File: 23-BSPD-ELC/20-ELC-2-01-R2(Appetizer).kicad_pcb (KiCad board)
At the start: 2 copper layers, 58 x 73 mm, 82 parts, among them J1 Conn_01x05, J2 Conn_01x03, SW1 UK-B0288-SP25Y, U1 LM239, U10 CD4043BDR, U2 LM239, U5 LM239, U6 SN74HC32PWR, U7 74HC04, U8 74HC08D,653, U9 74LVC2G17

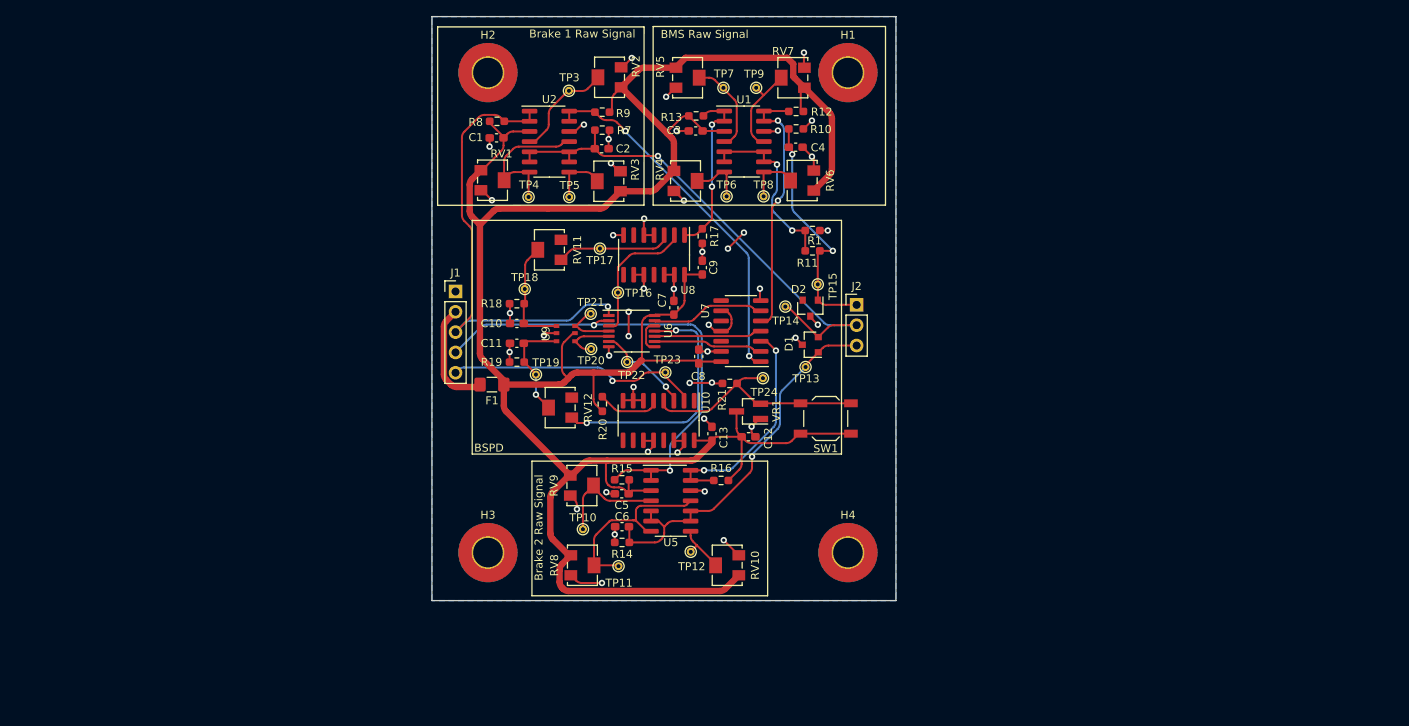
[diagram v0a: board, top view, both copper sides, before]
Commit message: Updated pcb layout; Watchdog on board still in progress
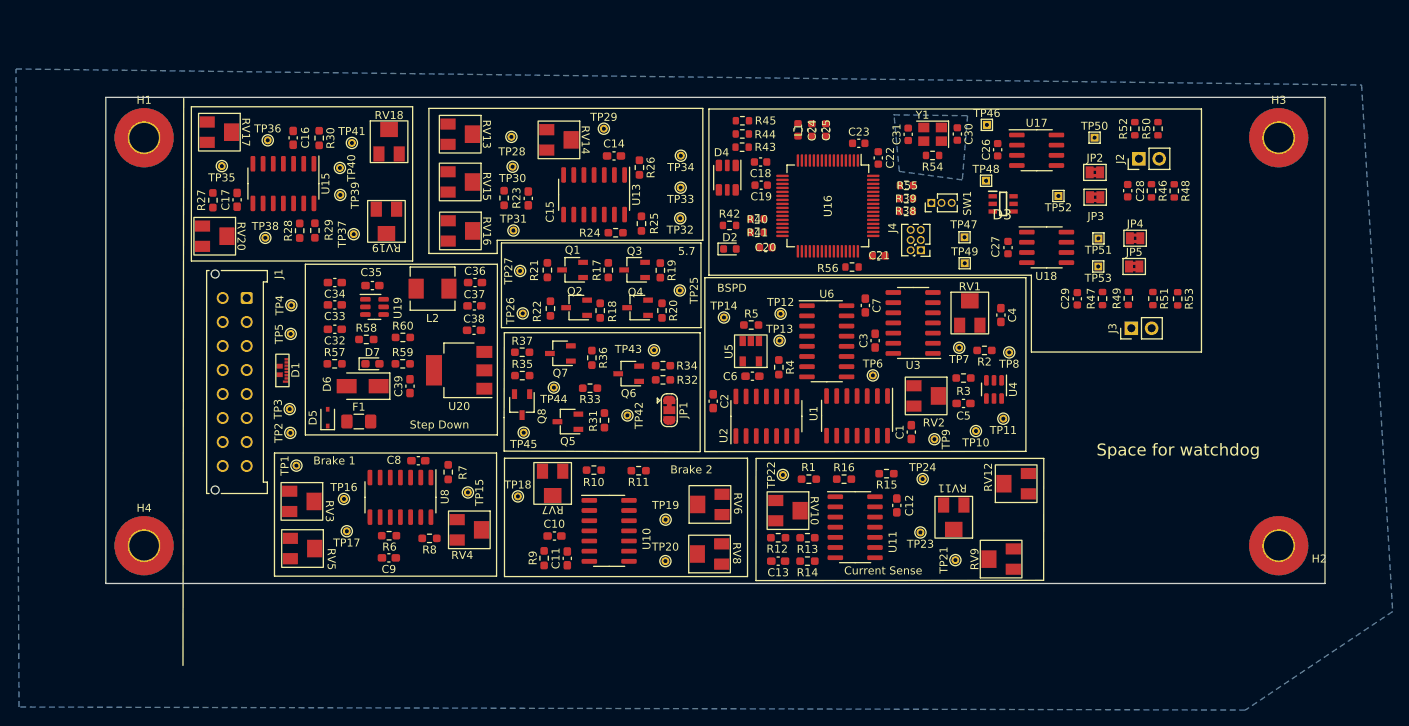
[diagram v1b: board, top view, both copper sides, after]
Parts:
- removed U7: 74HC04, Package_SO:SO-14_3.9x8.65mm_P1.27mm
- removed U9: 74LVC2G17, LHRE Footprint Library:74LVC2G17
- removed VR1: IMP810JEUR_T, Package_TO_SOT_SMD:SOT-23_Handsoldering
- added C14: 0.1uF, Capacitor_SMD:C_0603_1608Metric_Pad1.08x0.95mm_HandSolder, F.Cu at (130.8, 69.4)
- added C15: 0.1uF, Capacitor_SMD:C_0603_1608Metric_Pad1.08x0.95mm_HandSolder, F.Cu at (120.0, 74.7)
- added C16: 0.1uF, Capacitor_SMD:C_0603_1608Metric_Pad1.08x0.95mm_HandSolder, F.Cu at (90.7, 67.2)
- added C17: 0.1uF, Capacitor_SMD:C_0603_1608Metric_Pad1.08x0.95mm_HandSolder, F.Cu at (83.6, 74.9)
- added C18: 4u7, Capacitor_SMD:C_0603_1608Metric, F.Cu at (149.1, 70.2)
- added C19: 100n, Capacitor_SMD:C_0603_1608Metric, F.Cu at (149.2, 73.1)
- added C20: 100n, Capacitor_SMD:C_0603_1608Metric, F.Cu at (149.7, 80.9)
- added C21: 100n, Capacitor_SMD:C_0603_1608Metric, F.Cu at (163.8, 81.9)
- added C22: 100n, Capacitor_SMD:C_0603_1608Metric, F.Cu at (163.8, 69.7)
- added C23: 100n, Capacitor_SMD:C_0603_1608Metric, F.Cu at (161.4, 67.8)
- added C24: 1u, Capacitor_SMD:C_0603_1608Metric, F.Cu at (155.5, 66.2)
- added C25: 10n, Capacitor_SMD:C_0603_1608Metric, F.Cu at (157.2, 66.2)
- added C26: 0u1, Capacitor_SMD:C_0603_1608Metric, F.Cu at (178.7, 68.6)
- added C27: 0u1, Capacitor_SMD:C_0603_1608Metric, F.Cu at (180.0, 80.9)
- added C28: 4.7n, Capacitor_SMD:C_0603_1608Metric, F.Cu at (195.0, 73.8)
- added C29: 4.7n, Capacitor_SMD:C_0603_1608Metric, F.Cu at (188.7, 87.3)
- added C30: 10p, Capacitor_SMD:C_0603_1608Metric, F.Cu at (173.7, 66.7)
- added C31: 10p, Capacitor_SMD:C_0603_1608Metric, F.Cu at (167.5, 66.7)
- added C32: 10uF, Capacitor_SMD:C_0603_1608Metric_Pad1.08x0.95mm_HandSolder, F.Cu at (95.9, 91.1)
- added C33: 10uF, Capacitor_SMD:C_0603_1608Metric_Pad1.08x0.95mm_HandSolder, F.Cu at (95.9, 88.0)
- added C34: 100nF, Capacitor_SMD:C_0603_1608Metric_Pad1.08x0.95mm_HandSolder, F.Cu at (95.9, 85.2)
- added C35: 100nF, Capacitor_SMD:C_0603_1608Metric_Pad1.08x0.95mm_HandSolder, F.Cu at (100.6, 85.6)
- added C36: 22uF, Capacitor_SMD:C_0603_1608Metric_Pad1.08x0.95mm_HandSolder, F.Cu at (113.4, 85.2)
- added C37: 22uF, Capacitor_SMD:C_0603_1608Metric_Pad1.08x0.95mm_HandSolder, F.Cu at (113.3, 88.2)
- added C38: 1uF, Capacitor_SMD:C_0603_1608Metric_Pad1.08x0.95mm_HandSolder, F.Cu at (113.3, 91.2)
- added C39: 22uF, Capacitor_SMD:C_0603_1608Metric_Pad1.08x0.95mm_HandSolder, F.Cu at (105.3, 98.2)
- added D3: DT1446-04TS-7, Global Libraries:SOT95P280X100-6N, F.Cu at (179.4, 75.4)
- added D4: SMLVN6RGB, LED_SMD:LED_ROHM_SMLVN6, F.Cu at (144.9, 72.1)
- added D5: 32V, Diode_SMD:D_SOD-323, F.Cu at (95.0, 102.1)
- added D6: 0.7dV, Diode_SMD:D_SMA, F.Cu at (99.3, 98.2)
- added D7: LED, LED_SMD:LED_0603_1608Metric_Pad1.05x0.95mm_HandSolder, F.Cu at (100.6, 95.4)
- added J3: Conn_01x02, Connector_PinHeader_2.54mm:PinHeader_1x02_P2.54mm_Vertical, F.Cu at (195.4, 91.0)
- added J4: SWD, Connector_PinHeader_1.27mm:PinHeader_2x03_P1.27mm_Vertical, F.Cu at (169.1, 81.2)
- added JP1: Jumper_3_Bridged12, Jumper:SolderJumper-3_P1.3mm_Bridged12_RoundedPad1.0x1.5mm, F.Cu at (137.7, 101.2)
- added JP2: , Jumper:SolderJumper-2_P1.3mm_Bridged2Bar_Pad1.0x1.5mm, F.Cu at (190.9, 71.5)
- added JP3: , Jumper:SolderJumper-2_P1.3mm_Bridged2Bar_Pad1.0x1.5mm, F.Cu at (190.9, 74.6)
- added JP4: , Jumper:SolderJumper-2_P1.3mm_Bridged2Bar_Pad1.0x1.5mm, F.Cu at (195.9, 79.7)
- added JP5: , Jumper:SolderJumper-2_P1.3mm_Bridged2Bar_Pad1.0x1.5mm, F.Cu at (195.8, 83.2)
- added L1: 68n, Inductor_SMD:L_0603_1608Metric, F.Cu at (153.8, 66.2)
- added L2: 4u7, Inductor_SMD:L_Sunlord_MWSA0518_5.4x5.2mm, F.Cu at (108.1, 86.0)
- added Q1: Q_PMOS_GSD, Package_TO_SOT_SMD:TSOT-23, F.Cu at (125.6, 83.7)
- added Q2: Q_PMOS_GSD, Package_TO_SOT_SMD:TSOT-23, F.Cu at (126.1, 88.4)
- added Q3: Q_NMOS_GSD-Device, Package_TO_SOT_SMD:TSOT-23, F.Cu at (133.3, 83.7)
- added Q4: Q_NMOS_GSD-Device, Package_TO_SOT_SMD:TSOT-23, F.Cu at (133.7, 88.4)
- added Q5: Q_NMOS_GSD-Device, Package_TO_SOT_SMD:TSOT-23, F.Cu at (125.0, 102.6)
- added Q6: Q_NMOS_GSD-Device, Package_TO_SOT_SMD:TSOT-23, F.Cu at (132.6, 96.6)
- added Q7: Q_PMOS_DSG, Package_TO_SOT_SMD:TSOT-23, F.Cu at (124.1, 94.1)
- added Q8: Q_PMOS_DSG, Package_TO_SOT_SMD:TSOT-23, F.Cu at (119.3, 100.5)
- added R2: 10k, Resistor_SMD:R_0603_1608Metric_Pad0.98x0.95mm_HandSolder, F.Cu at (177.1, 93.7)
- added R22: 10k, Resistor_SMD:R_0603_1608Metric_Pad0.98x0.95mm_HandSolder, F.Cu at (122.8, 88.5)
- added R23: 510, Resistor_SMD:R_0603_1608Metric_Pad0.98x0.95mm_HandSolder, F.Cu at (117.0, 74.7)
- added R24: 10k, Resistor_SMD:R_0603_1608Metric_Pad0.98x0.95mm_HandSolder, F.Cu at (131.0, 79.0)
- added R25: 10k, Resistor_SMD:R_0603_1608Metric_Pad0.98x0.95mm_HandSolder, F.Cu at (134.2, 77.9)
- added R26: 10k, Resistor_SMD:R_0603_1608Metric_Pad0.98x0.95mm_HandSolder, F.Cu at (133.9, 70.9)
- added R27: 510, Resistor_SMD:R_0603_1608Metric_Pad0.98x0.95mm_HandSolder, F.Cu at (80.6, 75.0)
- added R28: 10k, Resistor_SMD:R_0603_1608Metric_Pad0.98x0.95mm_HandSolder, F.Cu at (91.5, 78.8)
- added R29: 10k, Resistor_SMD:R_0603_1608Metric_Pad0.98x0.95mm_HandSolder, F.Cu at (93.4, 78.7)
- added R3: 10k, Resistor_SMD:R_0603_1608Metric_Pad0.98x0.95mm_HandSolder, F.Cu at (174.4, 97.2)
- added R30: 10k, Resistor_SMD:R_0603_1608Metric_Pad0.98x0.95mm_HandSolder, F.Cu at (93.9, 67.2)
- added R31: 25, Resistor_SMD:R_0603_1608Metric_Pad0.98x0.95mm_HandSolder, F.Cu at (129.6, 102.5)
- added R32: 25, Resistor_SMD:R_0603_1608Metric_Pad0.98x0.95mm_HandSolder, F.Cu at (136.9, 97.4)
- added R33: 10k, Resistor_SMD:R_0603_1608Metric_Pad0.98x0.95mm_HandSolder, F.Cu at (127.8, 98.5)
- added R34: 10k, Resistor_SMD:R_0603_1608Metric_Pad0.98x0.95mm_HandSolder, F.Cu at (136.9, 95.6)
- added R35: 10k, Resistor_SMD:R_0603_1608Metric_Pad0.98x0.95mm_HandSolder, F.Cu at (119.3, 96.9)
- added R36: 10k, Resistor_SMD:R_0603_1608Metric_Pad0.98x0.95mm_HandSolder, F.Cu at (128.0, 94.7)
- added R37: 25, Resistor_SMD:R_0603_1608Metric_Pad0.98x0.95mm_HandSolder, F.Cu at (119.3, 94.0)
- added R38: 2k2, Resistor_SMD:R_0603_1608Metric, F.Cu at (167.3, 76.3)
- added R39: 2k2, Resistor_SMD:R_0603_1608Metric, F.Cu at (167.3, 74.7)
- added R4: 10k, Resistor_SMD:R_0603_1608Metric_Pad0.98x0.95mm_HandSolder, F.Cu at (151.4, 95.8)
- added R40: 2k2, Resistor_SMD:R_0603_1608Metric, F.Cu at (148.7, 77.3)
- added R41: 2k2, Resistor_SMD:R_0603_1608Metric, F.Cu at (148.7, 79.0)
- added R42: 100, Resistor_SMD:R_0603_1608Metric, F.Cu at (145.2, 78.1)
- added R43: 220, Resistor_SMD:R_0603_1608Metric, F.Cu at (146.8, 68.3)
- added R44: 220, Resistor_SMD:R_0603_1608Metric, F.Cu at (146.8, 66.7)
- added R45: 220, Resistor_SMD:R_0603_1608Metric, F.Cu at (146.8, 65.0)
- added R46: 120, Resistor_SMD:R_0603_1608Metric, F.Cu at (197.9, 73.8)
- added R47: 120, Resistor_SMD:R_0603_1608Metric, F.Cu at (191.8, 87.2)
- added R48: 120, Resistor_SMD:R_0603_1608Metric, F.Cu at (200.8, 73.8)
- added R49: 120, Resistor_SMD:R_0603_1608Metric, F.Cu at (195.0, 87.2)
- added R5: 100k, Resistor_SMD:R_0603_1608Metric_Pad0.98x0.95mm_HandSolder, F.Cu at (147.9, 90.6)
- added R50: 120, Resistor_SMD:R_0603_1608Metric, F.Cu at (198.8, 66.0)
- added R51: 120, Resistor_SMD:R_0603_1608Metric, F.Cu at (198.1, 87.2)
- added R52: 120, Resistor_SMD:R_0603_1608Metric, F.Cu at (195.9, 66.0)
- added R53: 120, Resistor_SMD:R_0603_1608Metric, F.Cu at (201.2, 87.3)
- added R54: 47, Resistor_SMD:R_0603_1608Metric, F.Cu at (170.6, 69.4)
- added R55: 10K, Resistor_SMD:R_0603_1608Metric, F.Cu at (167.3, 73.1)
- added R56: 22, Resistor_SMD:R_0603_1608Metric, F.Cu at (160.5, 83.3)
- added R57: 470R, Resistor_SMD:R_0603_1608Metric_Pad0.98x0.95mm_HandSolder, F.Cu at (95.8, 95.4)
- added R58: 10K, Resistor_SMD:R_0603_1608Metric_Pad0.98x0.95mm_HandSolder, F.Cu at (99.8, 92.4)
- added R59: 10K, Resistor_SMD:R_0603_1608Metric_Pad0.98x0.95mm_HandSolder, F.Cu at (104.3, 95.4)
- added R6: 510k, Resistor_SMD:R_0603_1608Metric_Pad0.98x0.95mm_HandSolder, F.Cu at (102.6, 116.9)
- added R60: 54.9K, Resistor_SMD:R_0603_1608Metric_Pad0.98x0.95mm_HandSolder, F.Cu at (104.4, 92.1)
- added RV13: 10k, Global Libraries:PVG5A, F.Cu at (111.5, 66.7)
- added RV14: 10k, Global Libraries:PVG5A, F.Cu at (123.9, 67.4)
- added RV15: R_POT_TRIM-Device, Global Libraries:PVG5A, F.Cu at (111.5, 72.7)
- added RV16: R_POT_TRIM-Device, Global Libraries:PVG5A, F.Cu at (111.6, 78.8)
- added RV17: 10k, Global Libraries:PVG5A, F.Cu at (81.4, 66.4)
- added RV18: 10k, Global Libraries:PVG5A, F.Cu at (102.6, 67.6)
- added RV19: R_POT_TRIM-Device, Global Libraries:PVG5A, F.Cu at (102.3, 77.6)
- added RV20: R_POT_TRIM-Device, Global Libraries:PVG5A, F.Cu at (80.8, 79.5)
- added TP1: TestPoint-Connector, TestPoint:TestPoint_THTPad_D1.0mm_Drill0.5mm, F.Cu at (91.1, 108.1)
- added TP2: TestPoint-Connector, TestPoint:TestPoint_THTPad_D1.0mm_Drill0.5mm, F.Cu at (90.3, 104.0)
- added TP25: TestPoint, TestPoint:TestPoint_THTPad_D1.0mm_Drill0.5mm, F.Cu at (139.0, 86.2)
- added TP26: TestPoint-Connector, TestPoint:TestPoint_THTPad_D1.0mm_Drill0.5mm, F.Cu at (119.4, 89.1)
- added TP27: TestPoint-Connector, TestPoint:TestPoint_THTPad_D1.0mm_Drill0.5mm, F.Cu at (119.0, 83.8)
- added TP28: TestPoint, TestPoint:TestPoint_THTPad_D1.0mm_Drill0.5mm, F.Cu at (117.9, 67.0)
- added TP29: TestPoint, TestPoint:TestPoint_THTPad_D1.0mm_Drill0.5mm, F.Cu at (129.5, 66.0)
- added TP30: TestPoint, TestPoint:TestPoint_THTPad_D1.0mm_Drill0.5mm, F.Cu at (118.1, 70.8)
- added TP31: TestPoint, TestPoint:TestPoint_THTPad_D1.0mm_Drill0.5mm, F.Cu at (118.2, 78.7)
- added TP32: TestPoint, TestPoint:TestPoint_THTPad_D1.0mm_Drill0.5mm, F.Cu at (139.0, 77.2)
- added TP33: TestPoint, TestPoint:TestPoint_THTPad_D1.0mm_Drill0.5mm, F.Cu at (139.1, 73.4)
- added TP34: TestPoint, TestPoint:TestPoint_THTPad_D1.0mm_Drill0.5mm, F.Cu at (139.1, 69.4)
- added TP35: TestPoint, TestPoint:TestPoint_THTPad_D1.0mm_Drill0.5mm, F.Cu at (81.7, 70.7)
- added TP36: TestPoint, TestPoint:TestPoint_THTPad_D1.0mm_Drill0.5mm, F.Cu at (87.5, 67.5)
- added TP37: TestPoint, TestPoint:TestPoint_THTPad_D1.0mm_Drill0.5mm, F.Cu at (98.2, 79.2)
- added TP38: TestPoint, TestPoint:TestPoint_THTPad_D1.0mm_Drill0.5mm, F.Cu at (87.2, 79.7)
- added TP39: TestPoint, TestPoint:TestPoint_THTPad_D1.0mm_Drill0.5mm, F.Cu at (96.5, 74.3)
- added TP40: TestPoint, TestPoint:TestPoint_THTPad_D1.0mm_Drill0.5mm, F.Cu at (96.5, 70.9)
- added TP41: TestPoint, TestPoint:TestPoint_THTPad_D1.0mm_Drill0.5mm, F.Cu at (98.0, 67.8)
- added TP42: TestPoint-Connector, TestPoint:TestPoint_THTPad_D1.0mm_Drill0.5mm, F.Cu at (132.4, 101.9)
- added TP43: TestPoint-Connector, TestPoint:TestPoint_THTPad_D1.0mm_Drill0.5mm, F.Cu at (135.8, 93.7)
- added TP44: TestPoint-Connector, TestPoint:TestPoint_THTPad_D1.0mm_Drill0.5mm, F.Cu at (123.2, 98.4)
- added TP45: TestPoint-Connector, TestPoint:TestPoint_THTPad_D1.0mm_Drill0.5mm, F.Cu at (119.5, 104.0)
- added TP46: , TestPoint:TestPoint_THTPad_1.0x1.0mm_Drill0.5mm, F.Cu at (177.4, 65.5)
- added TP47: , TestPoint:TestPoint_THTPad_1.0x1.0mm_Drill0.5mm, F.Cu at (174.6, 79.6)
- added TP48: , TestPoint:TestPoint_THTPad_1.0x1.0mm_Drill0.5mm, F.Cu at (177.3, 72.5)
- added TP49: , TestPoint:TestPoint_THTPad_1.0x1.0mm_Drill0.5mm, F.Cu at (174.6, 82.8)
- added TP50: , TestPoint:TestPoint_THTPad_1.0x1.0mm_Drill0.5mm, F.Cu at (190.8, 67.1)
- added TP51: , TestPoint:TestPoint_THTPad_1.0x1.0mm_Drill0.5mm, F.Cu at (191.3, 79.7)
- added TP52: , TestPoint:TestPoint_THTPad_1.0x1.0mm_Drill0.5mm, F.Cu at (186.3, 74.4)
- added TP53: , TestPoint:TestPoint_THTPad_1.0x1.0mm_Drill0.5mm, F.Cu at (191.3, 83.2)
- added U11: LM239, Package_SO:SO-14_3.9x8.65mm_P1.27mm, F.Cu at (160.9, 115.8)
- added U13: LM239, Package_SO:SO-14_3.9x8.65mm_P1.27mm, F.Cu at (128.3, 74.3)
- added U15: LM239, Package_SO:SO-14_3.9x8.65mm_P1.27mm, F.Cu at (89.4, 72.9)
- added U16: STM32F105RCTx, Package_QFP:LQFP-64_10x10mm_P0.5mm, F.Cu at (157.5, 75.7)
- added U17: SN65HVD230, Package_SO:SOIC-8_3.9x4.9mm_P1.27mm, F.Cu at (183.6, 68.7)
- added U18: SN65HVD230, Package_SO:SOIC-8_3.9x4.9mm_P1.27mm, F.Cu at (184.8, 80.8)
- added U19: LMR51420, Package_TO_SOT_SMD:SOT-23-6, F.Cu at (100.8, 88.3)
- added U20: AMS1117-3.3, Package_TO_SOT_SMD:SOT-223-3_TabPin2, F.Cu at (111.4, 96.2)
- added U3: 74HC08D,653, Package_SO:SOIC-14_3.9x8.7mm_P1.27mm, F.Cu at (168.1, 90.3)
- added U4: 74LVC2G17DBVE4, Package_TO_SOT_SMD:SOT-23-6, F.Cu at (178.3, 98.6)
- added Y1: 16MHz, Crystal:Crystal_SMD_3225-4Pin_3.2x2.5mm, F.Cu at (170.6, 66.7)
- C10, C11: value 1uF -> 0.1uF
- C4, C5: value 0.1uF -> 22uF
- D1: value PSM712-LF-T7 -> ESD7016MUTAG; footprint Package_TO_SOT_SMD:SOT-23 -> Global Libraries:ESD7016MUTAG
- D2: value PSM712-LF-T7 -> RED; footprint Package_TO_SOT_SMD:SOT-23 -> LED_SMD:LED_0603_1608Metric
- F1: value 1A -> 2A
- J1: value Conn_01x05 -> Conn_02x08_Counter_Clockwise; footprint Connector_PinHeader_2.54mm:PinHeader_1x05_P2.54mm_Vertical -> Connector_Molex:Molex_Micro-Fit_3.0_43045-1612_2x08_P3.00mm_Vertical
- J2: value Conn_01x03 -> Conn_01x02; footprint Connector_PinHeader_2.54mm:PinHeader_1x03_P2.54mm_Vertical -> Connector_PinHeader_2.54mm:PinHeader_1x02_P2.54mm_Vertical
- R1, R11: value 150 -> 10k
- R10, R7: value 510k -> 10k
- R12, R9: value 10k -> 510k
- R13: value 10k -> 150
- R14: value 510k -> 150
- R18, R19: value 10k -> 250
- RV1, RV10, RV11, RV12, RV2, RV3, RV4, RV5, RV6, RV7, RV8, RV9: footprint Potentiometer_SMD:Potentiometer_Bourns_3214W_Vertical -> Global Libraries:PVG5A
- SW1: value UK-B0288-SP25Y -> SW_SPDT; footprint Button_Switch_SMD:SW_SPST_TL3342 -> Connector_PinHeader_1.27mm:PinHeader_1x03_P1.27mm_Vertical
- TP3, TP4, TP5: value TestPoint -> TestPoint-Connector
- U1: value LM239 -> SN74ALS32DR; footprint Package_SO:SO-14_3.9x8.65mm_P1.27mm -> Package_SO:SOIC-14_3.9x8.7mm_P1.27mm
- U10: value CD4043BDR -> LM239; footprint Package_SO:SOIC-16_3.9x9.9mm_P1.27mm -> Package_SO:SO-14_3.9x8.65mm_P1.27mm
- U2: value LM239 -> 74HC04D,653
- U5: value LM239 -> APX823-44W5G-7; footprint Package_SO:SO-14_3.9x8.65mm_P1.27mm -> Global Libraries:AXP823-44W5G-7
- U6: value SN74HC32PWR -> CD4043BDR; footprint Package_SO:TSSOP-14_4.4x5mm_P0.65mm -> Package_SO:SOIC-16_3.9x9.9mm_P1.27mm
- U8: value 74HC08D,653 -> LM239; footprint Package_SO:SOIC-14_3.9x8.7mm_P1.27mm -> Package_SO:SO-14_3.9x8.65mm_P1.27mm
- moved H2 115.2 mm to (213.8, 118.1)
- moved H3 111.6 mm to (213.8, 67.1)
- moved H1 88.4 mm to (72.0, 67.1)
- moved H4 88.0 mm to (72.0, 118.1)
- moved RV5 76.0 mm to (91.8, 118.5), turned to -90 degrees
- moved D1 66.1 mm to (89.3, 96.2), turned to 90 degrees
- moved C1 63.6 mm to (167.9, 103.9), turned to 90 degrees
- moved RV1 61.9 mm to (175.2, 89.1), turned to 0 degrees
- moved RV11 60.6 mm to (173.2, 114.6), turned to 180 degrees
- moved RV7 58.9 mm to (123.1, 110.4), turned to 180 degrees
- moved RV12 57.8 mm to (181.0, 110.4), turned to 90 degrees
- moved R9 56.2 mm to (122.0, 119.7), turned to -90 degrees
- moved RV2 56.1 mm to (169.8, 99.4)
- moved RV3 55.4 mm to (91.7, 112.6)
- moved TP21 55.0 mm to (173.4, 119.9), turned to 90 degrees
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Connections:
- C10 pad 1: Net-(C10-Pad1) -> +5V
- C11 pad 1: Net-(C11-Pad1) -> /Brake2_Signal_Raw
- C13 pad 1: +5V -> /Current_Sense_Signal_Raw
- C2 pad 1: /Brake1_Signal_Raw -> +5V
- C4 pad 1: /BMS_Signal_Raw -> Net-(C4-Pad1)
- C5 pad 1: +5V -> Net-(C5-Pad1)
- C6 pad 1: /Brake2_Signal_Raw -> +5V
- C9 pad 1: +5V -> /Brake1_Signal_Raw
- D1 pad 1: /Brake2_Signal_Raw -> /Current_Sense_Signal_Raw
- D1 pad 2: /Brake1_Signal_Raw -> /Brake2_Signal_Raw
- D2 pad 1: /BMS_Signal_Raw -> Net-(D2-Pad1)
- D2 pad 2: unconnected-(D2-Pad2) -> +3V3
- F1 pad 1: +5V -> /24 to 5V Step Down/DIODE
- F1 pad 2: Net-(F1-Pad2) -> +24V
- J1 pad 1: GND -> +24V
- J1 pad 2: Net-(F1-Pad2) -> /APPs1_Signal_Raw
- J1 pad 3: /Brake1_Signal -> /APPs2_Signal_Raw
- J1 pad 4: /Brake2_Signal -> /Brake1_Signal_Raw
- J1 pad 5: /~{BSPD_TRIPPED} -> /Brake2_Signal_Raw
- J2 pad 1: /BMS_Signal_Raw -> Net-(C28-Pad2)
- J2 pad 2: /Brake1_Signal_Raw -> Net-(J2-Pad2)
- R1 pad 1: /BMS Signal/DataRaw_Half -> /CurrentSense_Signal
- R10 pad 1: GND -> /Brake2_Signal
- R10 pad 2: /BMS_Signal_Raw -> +5V
- R11 pad 1: /BMS Signal/DataRaw_Half -> +5V
- R11 pad 2: /BMS_Signal_Raw -> /Brake2_Connected
- R12 pad 1: /BMS_Connected -> GND
- R12 pad 2: +5V -> /Current_Sense_Signal_Raw
- R13 pad 1: +5V -> /BMS Signal/DataRaw_Half
- R13 pad 2: /BMS_Signal -> /Current_Sense_Signal_Raw
- R14 pad 1: GND -> /BMS Signal/DataRaw_Half
- R14 pad 2: /Brake2_Signal_Raw -> GND
- R15 pad 1: /Brake2_Signal -> /CurrentSense_Connected
- R16 pad 2: /Brake2_Connected -> /CurrentSense_Signal
- R17 pad 1: /BMS_Signal -> Net-(Q1-Pad1)
- R17 pad 2: GND -> /APPs1_Signal_Raw
- R18 pad 1: Net-(C10-Pad1) -> Net-(Q2-Pad1)
- R18 pad 2: GND -> /APPs2_Signal_Raw
- R19 pad 1: Net-(C11-Pad1) -> GND
- R19 pad 2: GND -> /5.7/APPS_Trip
- R20 pad 1: Net-(R20-Pad1) -> GND
- R20 pad 2: +5V -> /5.7/APPS_Trip
- R21 pad 1: /BrakeSystemPlausibilityDevice/SET -> GND
- R21 pad 2: GND -> /APPs1_Out
- R7 pad 1: GND -> /Brake1_Signal
- R7 pad 2: /Brake1_Signal_Raw -> +5V
- R8 pad 1: /Brake1_Signal -> +5V
- R8 pad 2: +5V -> /Brake1_Connected
- R9 pad 1: +5V -> GND
- R9 pad 2: /Brake1_Connected -> /Brake2_Signal_Raw
- RV1 pad 1: +5V -> /BrakeSystemPlausibilityDevice/Power_and_Brakes
- RV1 pad 2: /Brake1 Signal/Vref_4V -> Net-(C4-Pad1)
- RV1 pad 3: GND -> unconnected-(RV1-Pad3)
- RV11 pad 1: /BrakeSystemPlausibilityDevice/Power_and_Brakes -> +5V
- RV11 pad 2: Net-(C10-Pad1) -> Net-(RV11-Pad2)
- RV11 pad 3: unconnected-(RV11-Pad3) -> GND
- RV12 pad 1: /BrakeSystemPlausibilityDevice/Signal_Lost -> +5V
- RV12 pad 2: Net-(C11-Pad1) -> Net-(RV12-Pad2)
- RV12 pad 3: unconnected-(RV12-Pad3) -> GND
- RV2 pad 1: +5V -> /BrakeSystemPlausibilityDevice/Signal_Lost
- RV2 pad 2: Net-(RV2-Pad2) -> Net-(C5-Pad1)
- RV2 pad 3: GND -> unconnected-(RV2-Pad3)
- RV3 pad 2: Net-(RV3-Pad2) -> /Brake1 Signal/Vref_4V
- RV6 pad 2: Net-(RV6-Pad2) -> /Brake2 Signal/Vref_4V
- RV8 pad 2: /Brake2 Signal/Vref_4V -> Net-(RV8-Pad2)
- SW1 pad 1: +5V -> +3V3
- SW1 pad 2: /BrakeSystemPlausibilityDevice/SET -> Net-(R55-Pad1)
- TP10 pad 1: Net-(RV9-Pad2) -> /BrakeSystemPlausibilityDevice/Signal_Lost_TRIP
- TP11 pad 1: /Brake2 Signal/Vref_4V -> /BrakeSystemPlausibilityDevice/Power_and_Brakes_TRIP
- TP12 pad 1: Net-(RV10-Pad2) -> /BrakeSystemPlausibilityDevice/TRIP
- TP13 pad 1: /Brake2_Signal_Raw -> /BrakeSystemPlausibilityDevice/SET
- TP14 pad 1: /Brake1_Signal_Raw -> /~{BSPD_TRIPPED}
- TP15 pad 1: /BMS_Signal_Raw -> Net-(RV4-Pad2)
- TP16 pad 1: Net-(TP16-Pad1) -> /Brake1 Signal/Vref_4V
- TP17 pad 1: /BrakeSystemPlausibilityDevice/Power_and_Brakes -> Net-(RV5-Pad2)
- TP18 pad 1: Net-(C10-Pad1) -> Net-(RV7-Pad2)
- TP19 pad 1: Net-(C11-Pad1) -> /Brake2 Signal/Vref_4V
- TP20 pad 1: /BrakeSystemPlausibilityDevice/Signal_Lost_TRIP -> Net-(RV8-Pad2)
- TP21 pad 1: /BrakeSystemPlausibilityDevice/Power_and_Brakes_TRIP -> Net-(RV9-Pad2)
- TP22 pad 1: /BrakeSystemPlausibilityDevice/TRIP -> Net-(RV10-Pad2)
- TP23 pad 1: /~{BSPD_TRIPPED} -> Net-(RV11-Pad2)
- TP24 pad 1: /BrakeSystemPlausibilityDevice/SET -> Net-(RV12-Pad2)
- TP3 pad 1: Net-(RV2-Pad2) -> /Brake2_Signal_Raw
- TP4 pad 1: /Brake1 Signal/Vref_4V -> /APPs1_Signal_Raw
- TP5 pad 1: Net-(RV3-Pad2) -> /APPs2_Signal_Raw
- TP6 pad 1: Net-(RV4-Pad2) -> Net-(TP6-Pad1)
- TP7 pad 1: Net-(RV5-Pad2) -> /BrakeSystemPlausibilityDevice/Power_and_Brakes
- TP8 pad 1: Net-(RV6-Pad2) -> Net-(C4-Pad1)
- TP9 pad 1: Net-(RV7-Pad2) -> Net-(C5-Pad1)
- U1 pad 1: /BMS_Signal -> /Brake1_Signal
- U1 pad 10: /BMS Signal/DataRaw_Half -> /BrakeSystemPlausibilityDevice/~{Brake2_Connected}
- U1 pad 11: Net-(RV7-Pad2) -> /BrakeSystemPlausibilityDevice/Signal_Lost
- U1 pad 12: GND -> /BrakeSystemPlausibilityDevice/~{Brake_Connected}
- U1 pad 13: /BMS_Connected -> /BrakeSystemPlausibilityDevice/~{CS_Connected}
- U1 pad 14: /BMS_Connected -> +5V
- U1 pad 2: /BMS_Signal -> /Brake2_Signal
- U1 pad 3: +5V -> Net-(TP6-Pad1)
- U1 pad 4: Net-(RV5-Pad2) -> /BrakeSystemPlausibilityDevice/Power_and_Brakes_TRIP
- U1 pad 5: /BMS Signal/DataRaw_Half -> /BrakeSystemPlausibilityDevice/Signal_Lost_TRIP
- U1 pad 6: /BMS Signal/DataRaw_Half -> /BrakeSystemPlausibilityDevice/TRIP
- U1 pad 7: Net-(RV4-Pad2) -> GND
- U1 pad 8: Net-(RV6-Pad2) -> /BrakeSystemPlausibilityDevice/~{Brake_Connected}
- U1 pad 9: /BMS Signal/DataRaw_Half -> /BrakeSystemPlausibilityDevice/~{Brake1_Connected}
- U10 pad 1: unconnected-(U10-Pad1) -> /Brake2_Signal
- U10 pad 10: unconnected-(U10-Pad10) -> /Brake2_Signal_Raw
- U10 pad 11: GND -> /Brake2 Signal/Vref_4V
- U10 pad 13: unconnected-(U10-Pad13) -> /Brake2_Connected
- U10 pad 14: GND -> /Brake2_Connected
- U10 pad 2: /~{BSPD_TRIPPED} -> /Brake2_Signal
- U10 pad 3: /BrakeSystemPlausibilityDevice/TRIP -> +5V
- U10 pad 4: /BrakeSystemPlausibilityDevice/SET -> Net-(RV7-Pad2)
- U10 pad 5: Net-(R20-Pad1) -> /Brake2_Signal_Raw
- U10 pad 6: GND -> /Brake2_Signal_Raw
- U10 pad 7: GND -> /Brake2 Signal/Vref_4V
- U10 pad 8: GND -> Net-(RV8-Pad2)
- U10 pad 9: unconnected-(U10-Pad9) -> /Brake2_Signal_Raw
- U2 pad 1: /Brake1_Signal -> /Brake1_Connected
- U2 pad 10: /Brake1_Signal_Raw -> unconnected-(U2-Pad10)
- U2 pad 11: /Brake1 Signal/Vref_4V -> GND
- U2 pad 12: GND -> unconnected-(U2-Pad12)
- U2 pad 13: /Brake1_Connected -> GND
- U2 pad 14: /Brake1_Connected -> +5V
- U2 pad 2: /Brake1_Signal -> /BrakeSystemPlausibilityDevice/~{Brake1_Connected}
- U2 pad 3: +5V -> /Brake2_Connected
- U2 pad 4: Net-(RV2-Pad2) -> /BrakeSystemPlausibilityDevice/~{Brake2_Connected}
- U2 pad 5: /Brake1_Signal_Raw -> /CurrentSense_Connected
- U2 pad 6: /Brake1_Signal_Raw -> /BrakeSystemPlausibilityDevice/~{CS_Connected}
- U2 pad 7: /Brake1 Signal/Vref_4V -> GND
- U2 pad 8: Net-(RV3-Pad2) -> /~{Brake2_Signal}
- U2 pad 9: /Brake1_Signal_Raw -> /Brake2_Signal
- U5 pad 1: /Brake2_Signal -> /BrakeSystemPlausibilityDevice/SET
- U5 pad 2: /Brake2_Signal -> GND
- U5 pad 3: +5V -> /BSPD_Reset
- U5 pad 4: Net-(RV9-Pad2) -> unconnected-(U5-Pad4)
- U5 pad 5: /Brake2_Signal_Raw -> +5V
- U6 pad 1: /Brake1_Signal -> unconnected-(U6-Pad1)
- U6 pad 10: /BrakeSystemPlausibilityDevice/~{Brake2_Connected} -> unconnected-(U6-Pad10)
- U6 pad 11: /BrakeSystemPlausibilityDevice/Signal_Lost -> GND
- U6 pad 12: /BrakeSystemPlausibilityDevice/~{Brake_Connected} -> GND
- U6 pad 13: /BrakeSystemPlausibilityDevice/~{BMS_Connected} -> unconnected-(U6-Pad13)
- U6 pad 14: +5V -> GND
- U6 pad 2: /Brake2_Signal -> /~{BSPD_TRIPPED}
- U6 pad 3: Net-(TP16-Pad1) -> /BrakeSystemPlausibilityDevice/TRIP
- U6 pad 4: /BrakeSystemPlausibilityDevice/Power_and_Brakes_TRIP -> /BrakeSystemPlausibilityDevice/SET
- U6 pad 5: /BrakeSystemPlausibilityDevice/Signal_Lost_TRIP -> Net-(R4-Pad1)
- U6 pad 6: /BrakeSystemPlausibilityDevice/TRIP -> GND
- U6 pad 8: /BrakeSystemPlausibilityDevice/~{Brake_Connected} -> GND
- U6 pad 9: /BrakeSystemPlausibilityDevice/~{Brake1_Connected} -> unconnected-(U6-Pad9)
- U8 pad 1: /BMS_Signal -> /Brake1_Signal
- U8 pad 10: GND -> /Brake1_Signal_Raw
- U8 pad 11: unconnected-(U8-Pad11) -> /Brake1 Signal/Vref_4V
- U8 pad 13: GND -> /Brake1_Connected
- U8 pad 14: +5V -> /Brake1_Connected
- U8 pad 2: Net-(TP16-Pad1) -> /Brake1_Signal
- U8 pad 3: /BrakeSystemPlausibilityDevice/Power_and_Brakes -> +5V
- U8 pad 4: GND -> Net-(RV4-Pad2)
- U8 pad 5: GND -> /Brake1_Signal_Raw
- U8 pad 6: unconnected-(U8-Pad6) -> /Brake1_Signal_Raw
- U8 pad 7: GND -> /Brake1 Signal/Vref_4V
- U8 pad 8: unconnected-(U8-Pad8) -> Net-(RV5-Pad2)
- U8 pad 9: GND -> /Brake1_Signal_Raw
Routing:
- net +5V: track 311.4 -> 0.00 mm
- net GND: track 99.6 -> 0.00 mm, vias 45 -> 0
- net /Brake1_Signal_Raw: track 66.0 -> 0.00 mm, vias 1 -> 0
- net /Brake2_Signal: track 62.0 -> 0.00 mm, vias 2 -> 0
- net /Brake1_Signal: track 58.5 -> 0.00 mm, vias 1 -> 0
- net /Brake2_Signal_Raw: track 48.7 -> 0.00 mm, vias 1 -> 0
- net /Brake1_Connected: track 45.5 -> 0.00 mm, vias 2 -> 0
- net /BMS_Connected: track 33.1 -> 0.00 mm, vias 2 -> 0
- net /~{BSPD_TRIPPED}: track 31.8 -> 0.00 mm, vias 1 -> 0
- net /BrakeSystemPlausibilityDevice/Signal_Lost: track 31.8 -> 0.00 mm, vias 2 -> 0
- net /BMS_Signal_Raw: track 30.4 -> 0.00 mm, vias 2 -> 0
- net /BrakeSystemPlausibilityDevice/SET: track 30.3 -> 0.00 mm
- net /Brake2_Connected: track 28.7 -> 0.00 mm, vias 2 -> 0
- net /Brake2 Signal/Vref_4V: track 24.7 -> 0.00 mm
- net /BMS Signal/DataRaw_Half: track 22.8 -> 0.00 mm, vias 2 -> 0
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- added copper zone on B.Cu, net (none)
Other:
- board size 58 x 73 mm -> 152.4 x 60.8 mm
- board text added: "5.7"
- board text added: "Brake 1"
- board text added: "Brake 2"
- board text added: "Current Sense"
- board text added: "Space for watchdog"
- board text added: "Step Down"
- board text removed: "BMS Raw Signal"
- board text removed: "BSPD 2022"
- board text removed: "Brake 1 Raw Signal"
- board text removed: "Brake 2 Raw Signal"
- board text removed: "Connectors 1"
- board text removed: "Connectors 2"
- board text removed: "Dakota Britton Kevin Mechler Kaitlyn Sloan"

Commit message: BSPD layout
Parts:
- removed J4: SWD, Connector_PinHeader_1.27mm:PinHeader_2x03_P1.27mm_Vertical
- removed JP5: , Jumper:SolderJumper-2_P1.3mm_Bridged2Bar_Pad1.0x1.5mm
- removed R53: 120, Resistor_SMD:R_0603_1608Metric
- removed R54: 47, Resistor_SMD:R_0603_1608Metric
- removed R55: 10K, Resistor_SMD:R_0603_1608Metric
- removed TP51, TP52, TP53: , TestPoint:TestPoint_THTPad_1.0x1.0mm_Drill0.5mm
- added C40: 22uF, Capacitor_SMD:C_0603_1608Metric_Pad1.08x0.95mm_HandSolder, F.Cu at (106.3, 101.1)
- added C41: 1uF, Capacitor_SMD:C_0603_1608Metric_Pad1.08x0.95mm_HandSolder, F.Cu at (114.1, 84.3)
- added C42: 22uF, Capacitor_SMD:C_0603_1608Metric_Pad1.08x0.95mm_HandSolder, F.Cu at (114.1, 87.8)
- added R61: 54.9K, Resistor_SMD:R_0603_1608Metric_Pad0.98x0.95mm_HandSolder, F.Cu at (100.8, 97.9)
- added U21: AMS1117-3.3, Package_TO_SOT_SMD:SOT-223-3_TabPin2, F.Cu at (108.7, 86.1)
- C27: value 0u1 -> 4.7n
- C28, C29: value 4.7n -> 10p
- C30: value 10p -> .1uF
- C31: value 10p -> 1uF
- C32: value 10uF -> .1uF; footprint Capacitor_SMD:C_0603_1608Metric_Pad1.08x0.95mm_HandSolder -> Capacitor_SMD:C_0603_1608Metric
- C33: footprint Capacitor_SMD:C_0603_1608Metric_Pad1.08x0.95mm_HandSolder -> Capacitor_SMD:C_0603_1608Metric
- C34: value 100nF -> .1uF; footprint Capacitor_SMD:C_0603_1608Metric_Pad1.08x0.95mm_HandSolder -> Capacitor_SMD:C_0603_1608Metric
- C35: value 100nF -> 10uF
- C36: value 22uF -> 10uF
- C37: value 22uF -> 100nF
- C38: value 1uF -> 100nF
- J3: value Conn_01x02 -> SWD; footprint Connector_PinHeader_2.54mm:PinHeader_1x02_P2.54mm_Vertical -> Connector:Tag-Connect_TC2030-IDC-FP_2x03_P1.27mm_Vertical
- JP4: value (none) -> Jumper_3_Bridged12; footprint Jumper:SolderJumper-2_P1.3mm_Bridged2Bar_Pad1.0x1.5mm -> Jumper:SolderJumper-3_P1.3mm_Bridged12_RoundedPad1.0x1.5mm
- R19: value 250 -> 10k
- R37: value 25 -> 2k2; footprint Resistor_SMD:R_0603_1608Metric_Pad0.98x0.95mm_HandSolder -> Resistor_SMD:R_0603_1608Metric
- R41: value 2k2 -> 100
- R42: value 100 -> 220
- R45: value 220 -> 120
- R49: value 120 -> 47
- R50: value 120 -> 10K
- R51: value 120 -> 22
- R52: value 120 -> 470R; footprint Resistor_SMD:R_0603_1608Metric -> Resistor_SMD:R_0603_1608Metric_Pad0.98x0.95mm_HandSolder
- R56: value 22 -> 100k
- R57: value 470R -> 10k; footprint Resistor_SMD:R_0603_1608Metric_Pad0.98x0.95mm_HandSolder -> Resistor_SMD:R_0603_1608Metric
- R58: value 10K -> 10k; footprint Resistor_SMD:R_0603_1608Metric_Pad0.98x0.95mm_HandSolder -> Resistor_SMD:R_0603_1608Metric
- R60: value 54.9K -> 10K
- U18: value SN65HVD230 -> MCP3428; footprint Package_SO:SOIC-8_3.9x4.9mm_P1.27mm -> Package_SO:SOIC-14_3.9x8.7mm_P1.27mm
- U19: value LMR51420 -> LSF0204QPWRQ1; footprint Package_TO_SOT_SMD:SOT-23-6 -> Package_SO:TSSOP-14_4.4x5mm_P0.65mm
- U20: value AMS1117-3.3 -> LMR51420; footprint Package_TO_SOT_SMD:SOT-223-3_TabPin2 -> Package_TO_SOT_SMD:SOT-23-6
- moved C33 105.4 mm to (201.1, 94.8), turned to 0 degrees
- moved R52 104.2 mm to (95.2, 93.1), turned to 180 degrees
- moved R57 101.1 mm to (196.8, 99.4), turned to -90 degrees
- moved R58 97.7 mm to (196.9, 103.5), turned to 90 degrees
- moved C32 97.3 mm to (192.4, 103.6), turned to -90 degrees
- moved C34 92.5 mm to (186.5, 103.5), turned to -90 degrees
- moved U19 89.3 mm to (189.5, 99.1), turned to 180 degrees
- moved R45 61.3 mm to (201.8, 92.1), turned to -90 degrees
- moved SW1 48.6 mm to (197.4, 115.7), turned to 180 degrees
- moved R37 48.3 mm to (164.8, 77.8), turned to 90 degrees
- moved R50 42.4 mm to (197.2, 108.4), turned to 180 degrees
- moved C30 40.5 mm to (201.1, 96.5), turned to 0 degrees
- moved R49 39.8 mm to (163.1, 63.4), turned to 0 degrees
- moved C31 36.0 mm to (189.3, 95.4), turned to 0 degrees
- moved C28 35.9 mm to (159.9, 66.1)
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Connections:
- net /5.7/microcontroller/CAN1_H renamed /5.7/CANH
- net /5.7/microcontroller/CAN1_L renamed /5.7/CANL
- C27 pad 1: +3V3 -> GND
- C27 pad 2: GND -> Net-(C27-Pad2)
- C28 pad 1: GND -> /5.7/microcontroller/HSE_in
- C28 pad 2: Net-(C28-Pad2) -> GND
- C29 pad 1: GND -> Net-(C29-Pad1)
- C29 pad 2: Net-(C29-Pad2) -> GND
- C30 pad 1: /5.7/microcontroller/HSE_in -> +5V
- C32 pad 1: /24 to 5V Step Down/BUCK/V_in -> +3V3
- C33 pad 1: /24 to 5V Step Down/BUCK/V_in -> +5V
- C34 pad 1: /24 to 5V Step Down/BUCK/V_in -> +5V
- C35 pad 1: /24 to 5V Step Down/BUCK/SW -> /24 to 5V Step Down/BUCK/V_in
- C35 pad 2: /24 to 5V Step Down/BUCK/VBST -> GND
- C36 pad 1: +5V -> /24 to 5V Step Down/BUCK/V_in
- C37 pad 1: +5V -> /24 to 5V Step Down/BUCK/V_in
- C38 pad 1: +5V -> /24 to 5V Step Down/BUCK/SW
- C38 pad 2: GND -> /24 to 5V Step Down/BUCK/VBST
- C39 pad 1: +3V3 -> +5V
- D3 pad 1: Net-(D3-Pad1) -> unconnected-(D3-Pad1)
- D3 pad 3: Net-(D3-Pad3) -> unconnected-(D3-Pad3)
- J2 pad 1: Net-(C28-Pad2) -> Net-(C27-Pad2)
- J3 pad 1: Net-(C29-Pad2) -> +3V3
- JP4 pad 1: Net-(D3-Pad3) -> unconnected-(JP4-Pad1)
- JP4 pad 2: /5.7/microcontroller/CAN2_H -> Net-(JP4-Pad2)
- Q1 pad 3: /APPs1_Out -> /5.7/APPs1_Out
- Q2 pad 3: /APPs2_Out -> /5.7/APPs2_Out
- Q7 pad 2: /Shutdown_IN -> Net-(Q7-Pad2)
- Q7 pad 3: Net-(Q7-Pad3) -> /Shutdown_IN
- Q8 pad 2: Net-(Q8-Pad2) -> /Shutdown_OUT
- Q8 pad 3: /Shutdown_OUT -> Net-(Q7-Pad2)
- R21 pad 2: /APPs1_Out -> /5.7/APPs1_Out
- R22 pad 2: /APPs2_Out -> /5.7/APPs2_Out
- R35 pad 1: Net-(Q8-Pad2) -> Net-(Q7-Pad2)
- R37 pad 1: Net-(Q7-Pad3) -> +3V3
- R37 pad 2: Net-(Q8-Pad2) -> /5.7/microcontroller/I2C1_SCL
- R38 pad 2: /5.7/microcontroller/I2C1_SCL -> /5.7/microcontroller/I2C1_SDA
- R39 pad 2: /5.7/microcontroller/I2C1_SDA -> /5.7/microcontroller/I2C2_SCL
- R40 pad 2: /5.7/microcontroller/I2C2_SCL -> /5.7/microcontroller/I2C2_SDA
- R41 pad 1: +3V3 -> Net-(D2-Pad1)
- R41 pad 2: /5.7/microcontroller/I2C2_SDA -> GND
- R42 pad 1: Net-(D2-Pad1) -> Net-(D4-Pad6)
- R42 pad 2: GND -> /5.7/microcontroller/LED_B
- R43 pad 1: Net-(D4-Pad6) -> Net-(D4-Pad5)
- R43 pad 2: /5.7/microcontroller/LED_B -> /5.7/microcontroller/LED_G
- R44 pad 1: Net-(D4-Pad5) -> Net-(D4-Pad4)
- R44 pad 2: /5.7/microcontroller/LED_G -> /5.7/microcontroller/LED_R
- R45 pad 1: Net-(D4-Pad4) -> Net-(C27-Pad2)
- R45 pad 2: /5.7/microcontroller/LED_R -> Net-(D3-Pad4)
- R46 pad 1: Net-(C28-Pad2) -> Net-(C27-Pad2)
- R47 pad 1: Net-(C29-Pad2) -> Net-(D3-Pad6)
- R47 pad 2: Net-(D3-Pad1) -> Net-(J2-Pad2)
- R48 pad 1: Net-(C28-Pad2) -> Net-(D3-Pad6)
- R48 pad 2: Net-(D3-Pad4) -> Net-(J2-Pad2)
- R49 pad 1: Net-(C29-Pad2) -> /5.7/microcontroller/HSE_out
- R49 pad 2: Net-(D3-Pad1) -> Net-(C29-Pad1)
- R50 pad 1: Net-(D3-Pad6) -> Net-(R50-Pad1)
- R50 pad 2: Net-(J2-Pad2) -> /5.7/microcontroller/BOOT0
- R51 pad 1: Net-(D3-Pad3) -> Net-(J3-Pad2)
- R51 pad 2: Net-(J3-Pad2) -> /5.7/microcontroller/SWDIO
- R52 pad 1: Net-(D3-Pad6) -> GND
- R52 pad 2: Net-(J2-Pad2) -> Net-(D7-Pad1)
- R56 pad 1: Net-(J4-Pad2) -> Net-(C31-Pad1)
- R56 pad 2: /5.7/microcontroller/SWDIO -> +3V3
- R57 pad 1: GND -> /Watchdog/SDA
- R57 pad 2: Net-(D7-Pad1) -> +5V
- R58 pad 1: /24 to 5V Step Down/BUCK/V_in -> /Watchdog/SCL
- R58 pad 2: /24 to 5V Step Down/BUCK/EN -> +5V
- R59 pad 1: /24 to 5V Step Down/BUCK/VFB -> /24 to 5V Step Down/BUCK/V_in
- R59 pad 2: GND -> /24 to 5V Step Down/BUCK/EN
- R60 pad 2: +5V -> GND
- SW1 pad 2: Net-(R55-Pad1) -> Net-(R50-Pad1)
- TP1 pad 1: /Brake1_Signal_Raw -> /Brake2_Signal_Raw
- TP2 pad 1: /Current_Sense_Signal_Raw -> /Brake1_Signal_Raw
- TP26 pad 1: /APPs2_Out -> /5.7/APPs2_Out
- TP27 pad 1: /APPs1_Out -> /5.7/APPs1_Out
- TP3 pad 1: /Brake2_Signal_Raw -> /Current_Sense_Signal_Raw
- TP44 pad 1: Net-(Q7-Pad3) -> Net-(Q7-Pad2)
- TP47 pad 1: /5.7/microcontroller/CAN2_TX -> /5.7/microcontroller/CAN1_RX
- TP48 pad 1: /5.7/microcontroller/CAN1_RX -> Net-(D3-Pad6)
- TP49 pad 1: /5.7/microcontroller/CAN2_RX -> Net-(D3-Pad4)
- U16 pad 33: /5.7/microcontroller/CAN2_RX -> unconnected-(U16-Pad33)
- U16 pad 34: /5.7/microcontroller/CAN2_TX -> unconnected-(U16-Pad34)
- U18 pad 1: /5.7/microcontroller/CAN2_TX -> /Watchdog/CH1+
- U18 pad 3: +3V3 -> /Watchdog/CH2+
- U18 pad 4: /5.7/microcontroller/CAN2_RX -> GND
- U18 pad 5: unconnected-(U18-Pad5) -> GND
- U18 pad 6: Net-(D3-Pad1) -> +5V
- U18 pad 7: Net-(D3-Pad3) -> /Watchdog/SDA
- U18 pad 8: GND -> /Watchdog/SCL
- U19 pad 1: GND -> +3V3
- U19 pad 2: /24 to 5V Step Down/BUCK/SW -> /Watchdog/A1
- U19 pad 3: /24 to 5V Step Down/BUCK/V_in -> Net-(JP4-Pad2)
- U19 pad 4: /24 to 5V Step Down/BUCK/VFB -> /Watchdog/A3
- U19 pad 5: /24 to 5V Step Down/BUCK/EN -> /Watchdog/A4
- U19 pad 6: /24 to 5V Step Down/BUCK/VBST -> (no net)
- U20 pad 2: +3V3 -> /24 to 5V Step Down/BUCK/SW
- U20 pad 3: +5V -> /24 to 5V Step Down/BUCK/V_in
- Y1 pad 3: Net-(C31-Pad1) -> Net-(C29-Pad1)
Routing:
- removed copper zone on B.Cu, net (none)
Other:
- board size 152.4 x 60.8 mm -> 143.6 x 61 mm
- board text removed: "Space for watchdog"
